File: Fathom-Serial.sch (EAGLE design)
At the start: 107 parts, among them IC1 LMH6643, IC2 LMH6643, IC3 ST490AB, IC4 ST490AB, IC5 FT230XS, Q1 BC817-40W, U1 MC7812, U2 MC7805, U4 INA139, U5 MC7805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

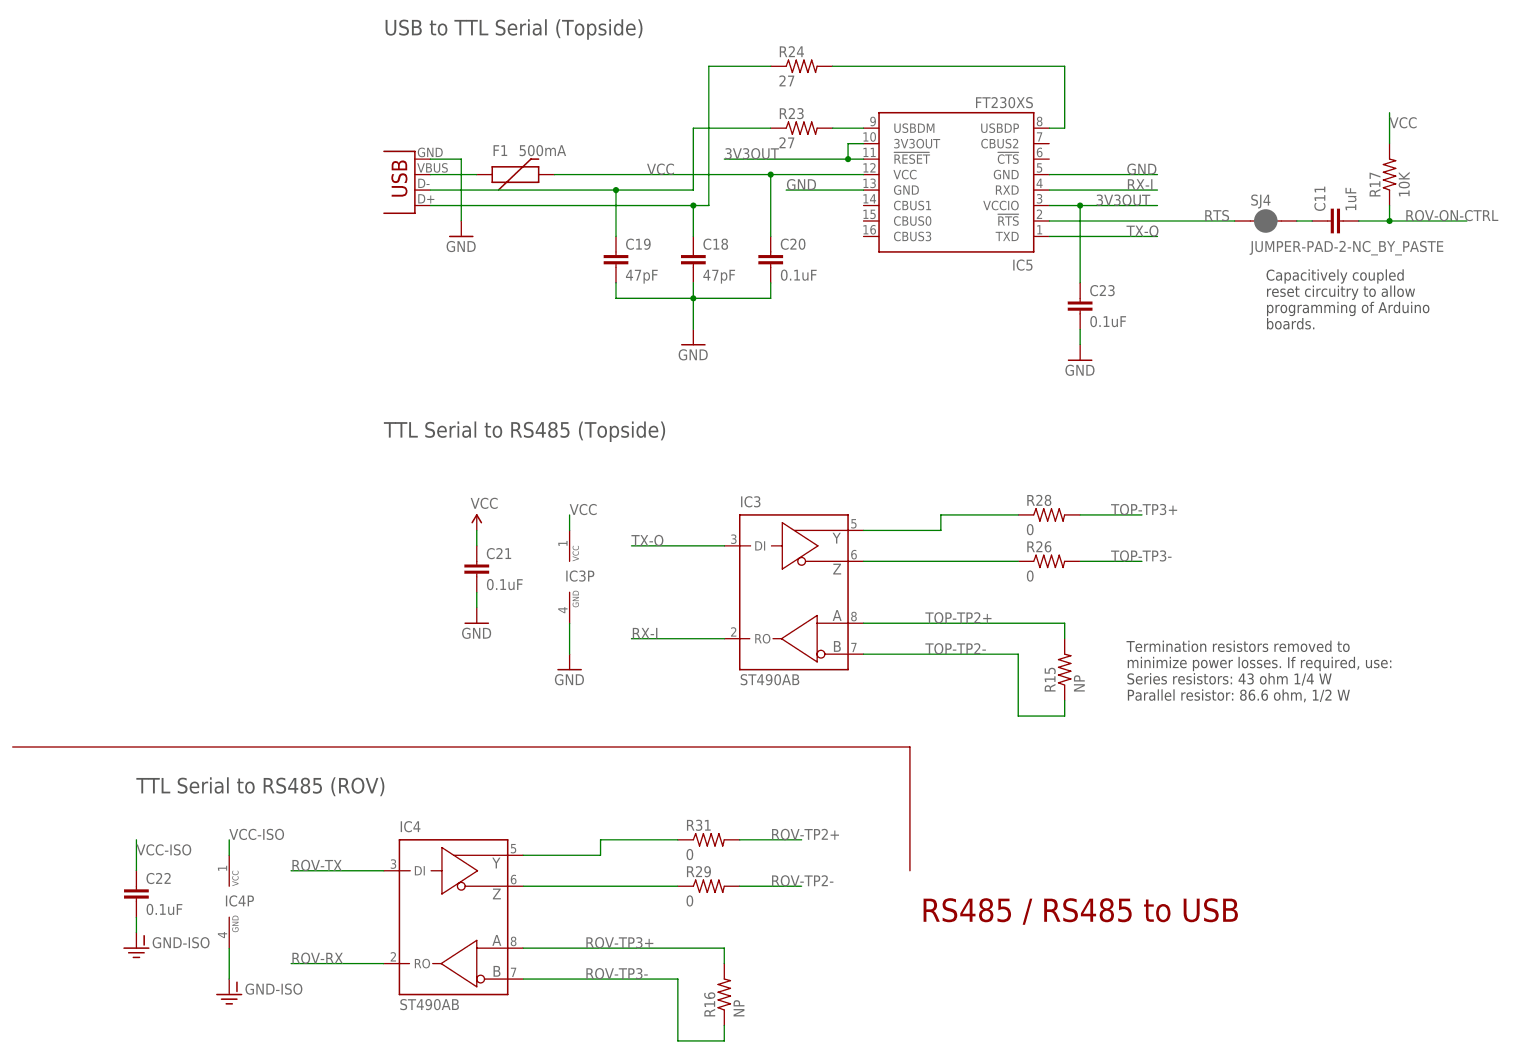
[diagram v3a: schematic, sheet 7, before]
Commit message: Updated schematic frames and changed references from 485 to 422.
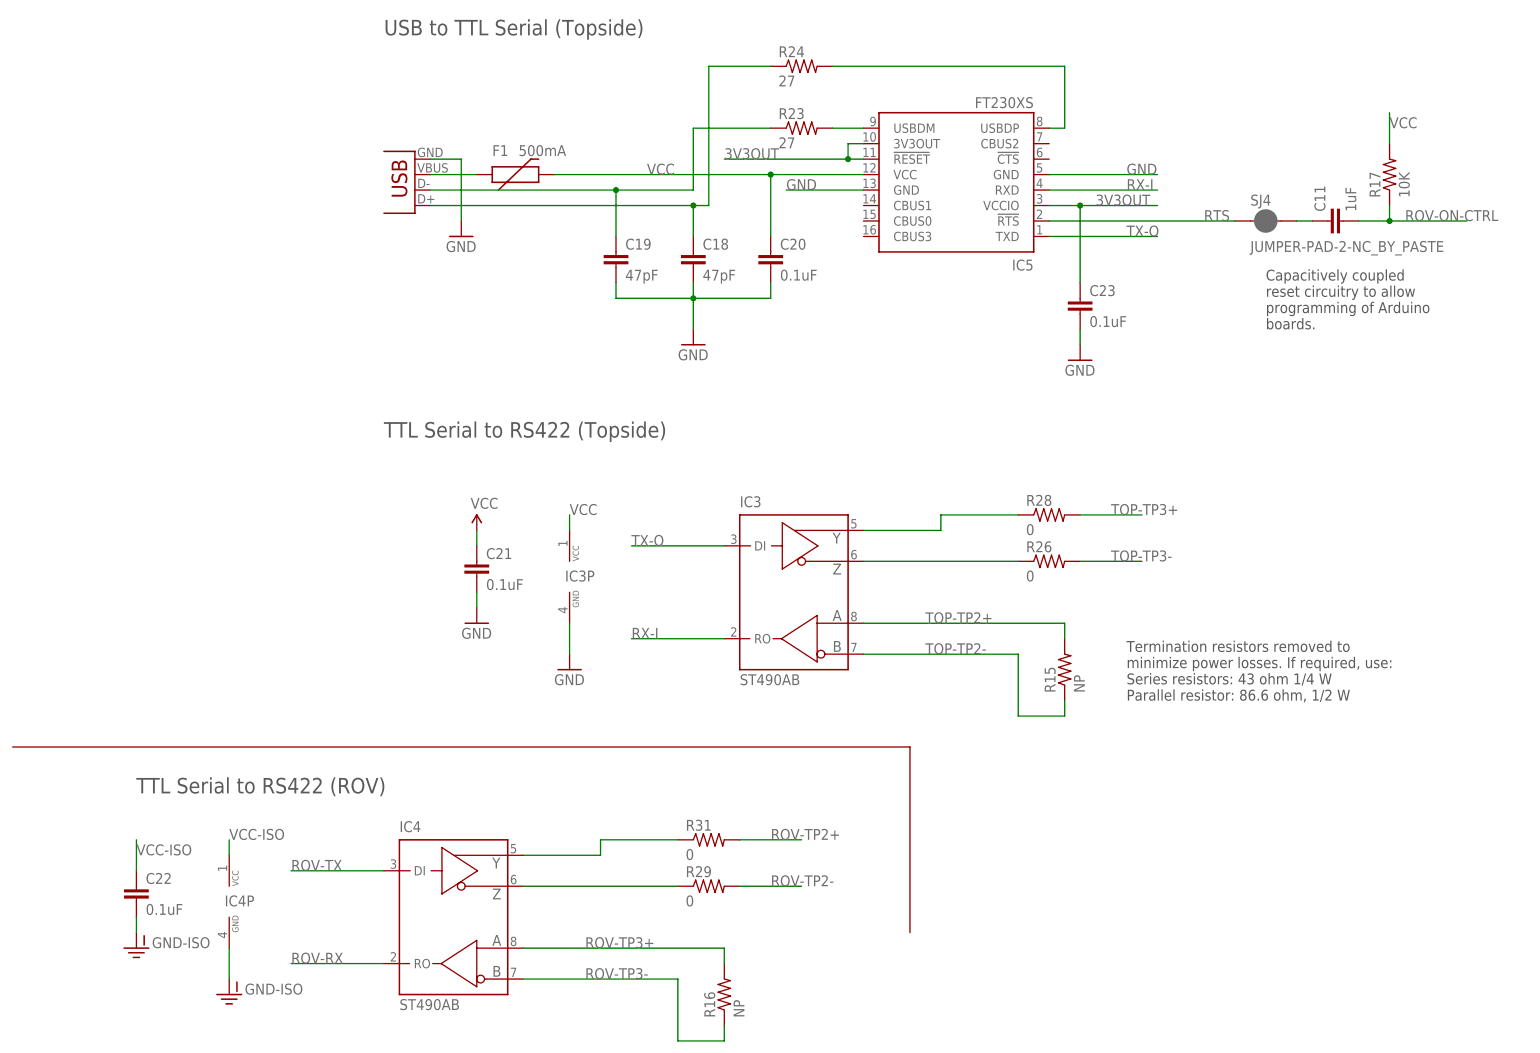
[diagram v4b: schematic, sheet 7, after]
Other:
- note added: "TTL Serial to RS422 (ROV)"
- note added: "TTL Serial to RS422 (Topside)"
- note removed: "Onboard Connectors & Misc."
- note removed: "Power"
- note removed: "ROV Power-on Switch"
- note removed: "RS485 / RS485 to USB"
- note removed: "TTL Serial to RS485 (ROV)"
- note removed: "TTL Serial to RS485 (Topside)"
- note removed: "Topside Connectors & Misc."
- note removed: "Video"
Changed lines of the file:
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@@
 <part name="D1" library="SparkFun-DiscreteSemi" deviceset="DIODE-ZENER" device="3.3V" value="16V"/>
 <part name="C13" library="SparkFun-Passives" deviceset="CAP_POL" device="6032" value="10uF 25V"/>
-<part name="FRAME1" library="frames" deviceset="LETTER_L" device=""/>
-<part name="FRAME2" library="frames" deviceset="LETTER_L" device=""/>
-<part name="FRAME3" library="frames" deviceset="LETTER_L" device=""/>
+<part name="FRAME1" library="BlueRobotics-Main" deviceset="FRAME-BLUEROBOTICS" device="" value="Onboard Connectors &amp; Misc."/>
+<part name="FRAME2" library="BlueRobotics-Main" deviceset="FRAME-BLUEROBOTICS" device="" value="Video Amplifiers"/>
+<part name="FRAME3" library="BlueRobotics-Main" deviceset="FRAME-BLUEROBOTICS" device="" value="Power"/>
 <part name="GND-ISO3" library="SparkFun-Aesthetics" deviceset="GND-ISO" device=""/>
-<part name="FRAME4" library="frames" deviceset="LETTER_L" device=""/>
-<part name="FRAME6" library="frames" deviceset="LETTER_L" device=""/>
+<part name="FRAME4" library="BlueRobotics-Main" deviceset="FRAME-BLUEROBOTICS" device="" value="RS422 / RS422 to USB"/>
+<part name="FRAME6" library="BlueRobotics-Main" deviceset="FRAME-BLUEROBOTICS" device="" value="ROV Power-on Switch"/>
 <part name="GND-ISO7" library="SparkFun-Aesthetics" deviceset="GND-ISO" device=""/>
 <part name="JP3" library="SparkFun-Connectors" deviceset="M03" device="PTH" value="0.1&quot; HEADER"/>
@@
 <part name="R36" library="SparkFun-Resistors" deviceset="33KOHM1/10W1%(0603)" device="" value="18K 1%"/>
 <part name="R37" library="SparkFun-Resistors" deviceset="33KOHM1/10W1%(0603)" device="" value="2.2K 1%"/>
-<part name="FRAME5" library="frames" deviceset="LETTER_L" device=""/>
+<part name="FRAME5" library="BlueRobotics-Main" deviceset="FRAME-BLUEROBOTICS" device="" value="Indicator LEDs"/>
 <part name="GND-ISO22" library="SparkFun-Aesthetics" deviceset="GND-ISO" device=""/>
 <part name="R38" library="SparkFun-Resistors" deviceset="33KOHM1/10W1%(0603)" device="" value="330"/>
@@
 <part name="SJ1" library="SparkFun-Passives" deviceset="JUMPER-PAD-3-2OF3_NC_BY_PASTE" device="" value=""/>
 <part name="JP10" library="SparkFun-Connectors" deviceset="M02" device="PTH" value="0.1&quot; HEADER"/>
-<part name="FRAME7" library="frames" deviceset="LETTER_L" device=""/>
+<part name="FRAME7" library="BlueRobotics-Main" deviceset="FRAME-BLUEROBOTICS" device="" value="Topside Connectors &amp; Misc."/>
 <part name="U$8" library="BR-Eagle-Library" deviceset="TETHER-HEADER" device="SERIAL" value="TETHER-HEADERSERIAL"/>
 <part name="U1" library="BR-Eagle-Library" deviceset="78XX" device="" value="MC7812"/>
@@
 <plain>
 <text x="15.24" y="177.8" size="2.54" layer="97">ROV Tether Terminal</text>
-<text x="149.098" y="27.178" size="3.81" layer="94">Onboard Connectors &amp; Misc.</text>
 <text x="106.68" y="177.8" size="2.54" layer="97">Power Terminal</text>
 <text x="106.68" y="96.52" size="2.54" layer="97">Camera Connections</text>
@@
 <sheet>
 <plain>
-<text x="149.098" y="27.178" size="3.81" layer="94">Topside Connectors &amp; Misc.</text>
 <text x="10.16" y="175.26" size="2.54" layer="97">Topside Tether Terminal</text>
 <text x="91.44" y="175.26" size="2.54" layer="97">Alternate TOP-VIN</text>
@@
 <sheet>
 <plain>
-<text x="149.098" y="27.178" size="3.81" layer="94">Power</text>
 <text x="7.62" y="177.8" size="2.54" layer="97">Supply Inverter for Op-Amp (ROV)</text>
 <text x="142.24" y="177.8" size="2.54" layer="97">Supply Inverter for Op-Amp (Topside)</text>
@@
 <sheet>
 <plain>
-<text x="149.098" y="27.178" size="3.81" layer="94">ROV Power-on Switch</text>
 <text x="30.48" y="162.56" size="2.54" layer="97">Power-on Switch</text>
 <text x="7.62" y="106.68" size="1.778" layer="97">ROV-ON between
@@
 <sheet>
 <plain>
-<text x="149.098" y="27.178" size="3.81" layer="94">Video</text>
 <text x="10.16" y="154.94" size="2.54" layer="97">NTSC to Differential (ROV)</text>
 <text x="134.62" y="154.94" size="2.54" layer="97">Differential to NTSC (Topside)</text>
@@
 <sheet>
 <plain>
-<text x="149.098" y="27.178" size="3.81" layer="94">RS485 / RS485 to USB</text>
 <text x="60.96" y="172.72" size="2.54" layer="97">USB to TTL Serial (Topside)</text>
-<text x="60.96" y="106.68" size="2.54" layer="97">TTL Serial to RS485 (Topside)</text>
-<text x="20.32" y="48.26" size="2.54" layer="97">TTL Serial to RS485 (ROV)</text>
-<wire x1="147.32" y1="35.56" x2="147.32" y2="55.88" width="0.1524" layer="94"/>
+<text x="60.96" y="106.68" size="2.54" layer="97">TTL Serial to RS422 (Topside)</text>
+<text x="20.32" y="48.26" size="2.54" layer="97">TTL Serial to RS422 (ROV)</text>
+<wire x1="147.32" y1="25.4" x2="147.32" y2="55.88" width="0.1524" layer="94"/>
 <wire x1="147.32" y1="55.88" x2="0" y2="55.88" width="0.1524" layer="94"/>
 <text x="182.88" y="63.5" size="1.778" layer="97">Termination resistors removed to
